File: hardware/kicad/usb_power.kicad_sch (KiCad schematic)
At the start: 14 parts, among them J1 U262-161N-4BVC11, U6 USBLC6-2P6, U7 MCP73831T-2ACI/OT

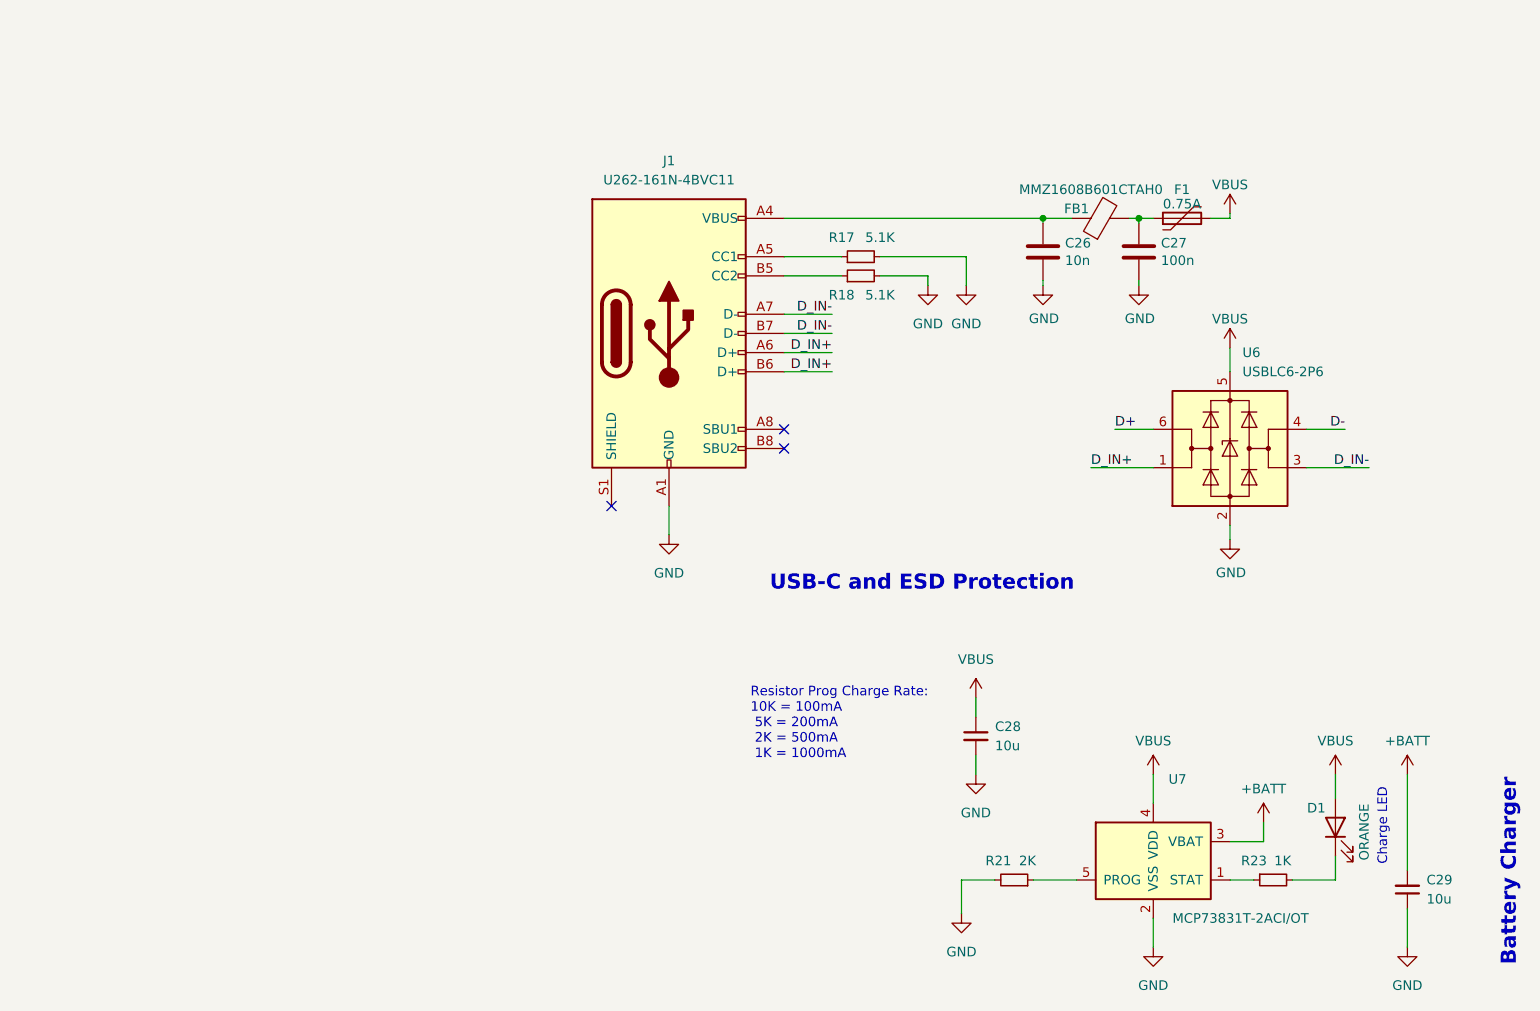
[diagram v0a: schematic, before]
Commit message: fix label
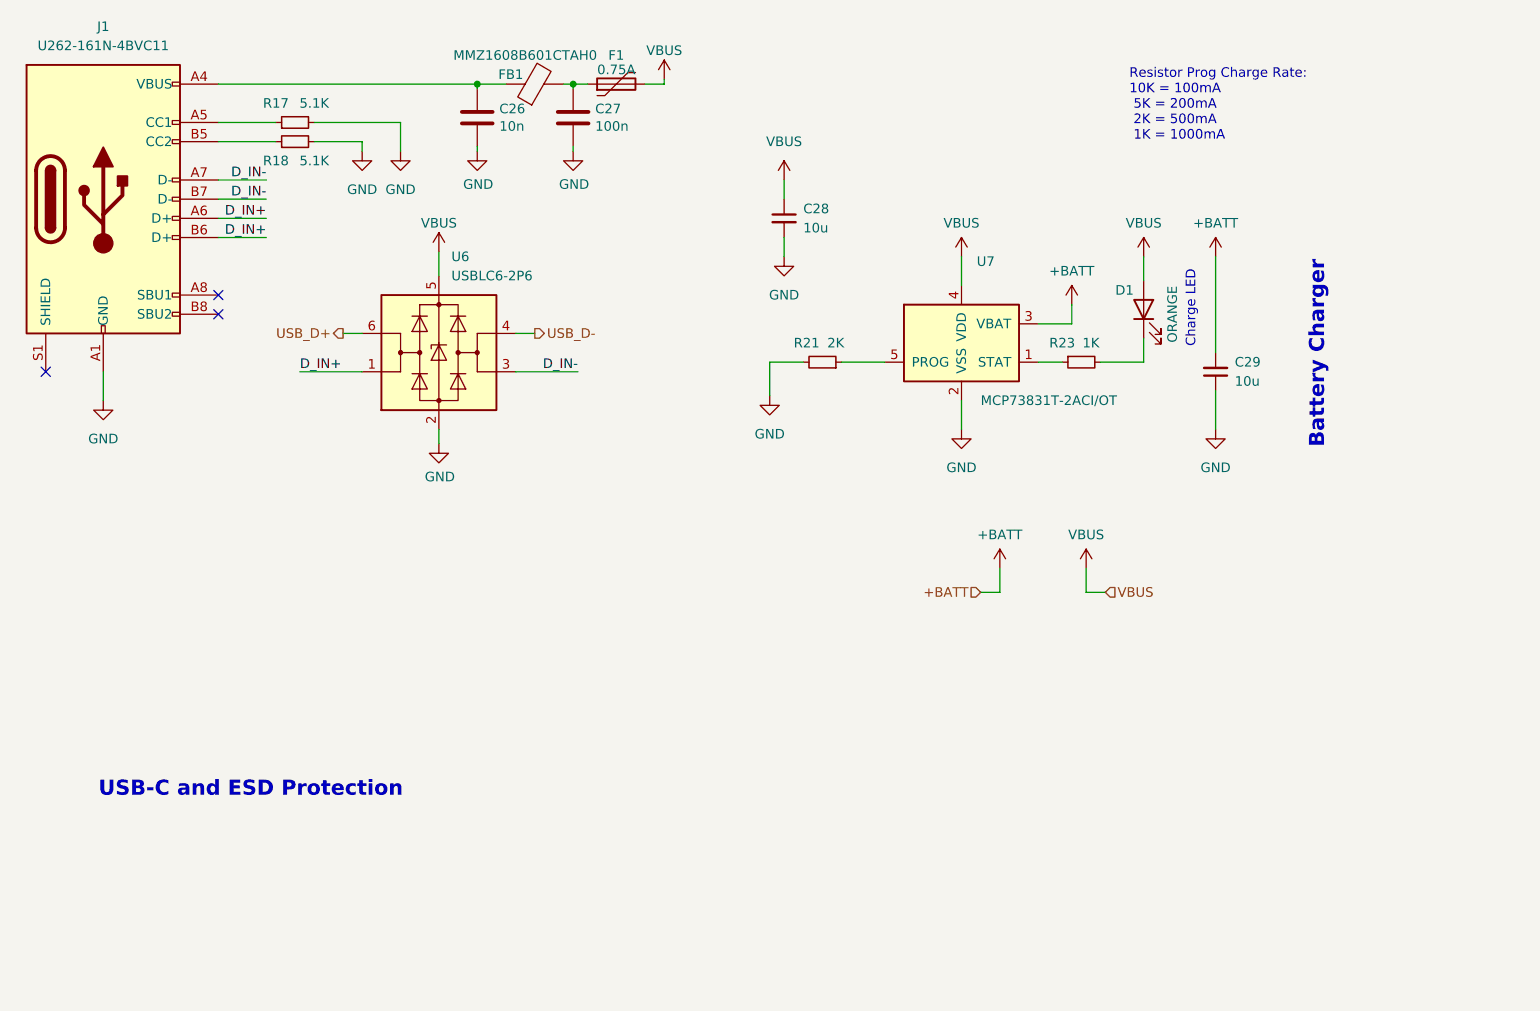
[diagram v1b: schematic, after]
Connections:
- net D+ renamed USB_D+
- net D- renamed USB_D-
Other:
- moved on the sheet: C26, C27, C28, C29, D1, F1, FB1, J1, R17, R18, R21, R23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

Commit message: beautify schematic
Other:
- note added: "Charge Rate: 500mA"
- note added: "Sheets Connection"
- note removed: "Resistor Prog Charge Rate: 10K = 100mA 5K = 200mA 2K = 500mA 1K = 1000mA"
- moved on the sheet: C26, C27, C28, C29, D1, F1, FB1, J1, R17, R18, R21, R23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

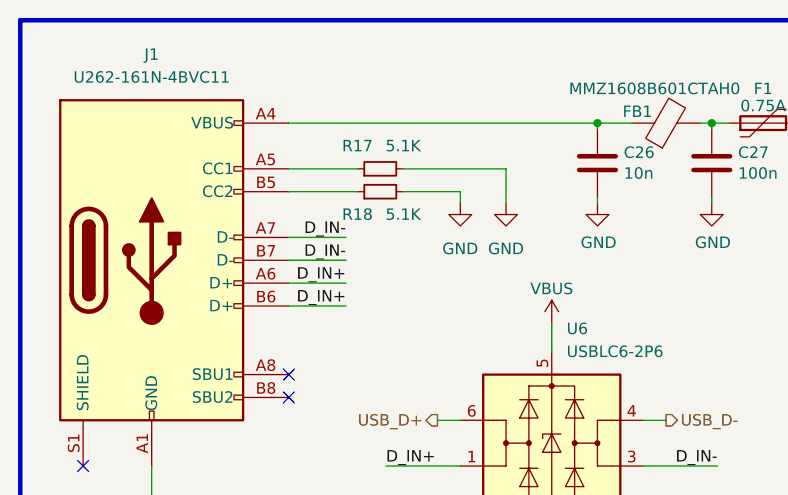
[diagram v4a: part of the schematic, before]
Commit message: usb power schematic partially done
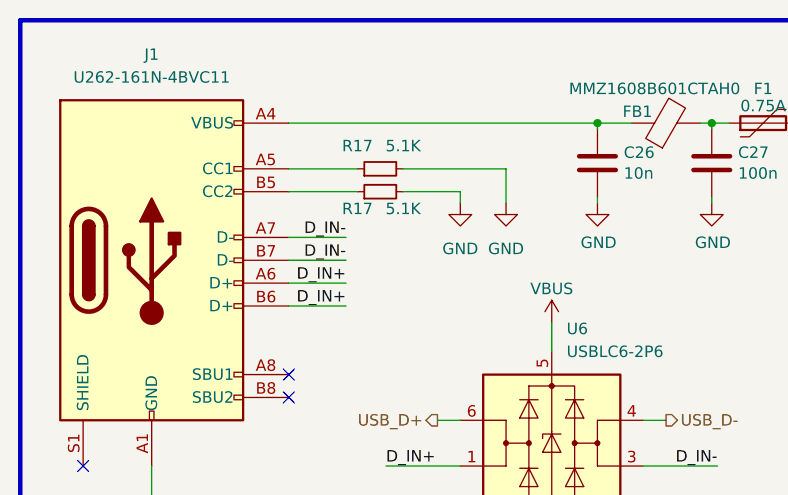
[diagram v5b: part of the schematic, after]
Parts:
- removed R18: 5.1K, Resistor_SMD:R_0402_1005Metric, symbol Device:R_Small
- added R17: 5.1K, Resistor_SMD:R_0402_1005Metric, symbol Device:R_Small
- C26: Distributor (none) -> LCSC; Distributor Link (none) -> https://www.lcsc.com/product-detail/Multilayer-Ceramic-Capa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; Distributor Part Number (none) -> C60133; Manufacturer Part Number (none) -> CC0402KRX7R9BB103; Part Description Ceramic Capacitor 10nF 10% 50V X7R -> Ceramic Capacitors 50V 10nF X7R ±10%; Part Number CC0402KRX7R9BB103 -> (none)
- C27: Distributor (none) -> LCSC; Distributor Link (none) -> https://www.lcsc.com/product-detail/Multilayer-Ceramic-Capa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; Distributor Part Number (none) -> C129131; Manufacturer Part Number (none) -> CC0402KRX5R6BB104; Part Description Ceramic Capacitor 100nF 10% 10V X5R -> Ceramic Capacitor 10V 100nF X5R ±10% 0402; Part Number CC0402KRX5R6BB104 -> (none)
- F1: Distributor (none) -> LCSC; Distributor Link (none) -> https://www.lcsc.com/product-detail/Resettable-Fuses_RUILON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; Distributor Part Number (none) -> C20979; Manufacturer RUILON -> RUILON(Shenzhen Ruilongyuan Elec); Manufacturer Part Number (none) -> SMD0805P075TF; Part Number SMD0805P075TF -> (none)
- FB1: Distributor (none) -> LCSC; Distributor Link (none) -> https://www.lcsc.com/product-detail/Ferrite-Beads_TDK-MMZ16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; Distributor Part Number (none) -> C97120; Manufacturer Part Number (none) -> MMZ1608B601CTAH0; Part Description (none) -> Ferrite Beads 400mΩ ±25% 600Ω@100MHz; Part Number MMZ1608B601CTAH0 -> (none)
- J1: footprint bwlr1e_prog:USB_C_Receptacle_XKB_U262-16XN-4BVC11 -> plantpal:USB_C_Receptacle_XKB_U262-16XN-4BVC11; Distributor (none) -> LCSC; Distributor Link (none) -> https://www.lcsc.com/product-detail/USB-Connectors_XKB-Conn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; Distributor Part Number (none) -> C319148; Manufacturer Part Number (none) -> U262-161N-4BVC11; Part Description (none) -> USB Connectors Type-C 3A USB 3.1 16P; Part Number U262-161N-4BVC11 -> (none)
- R17: Distributor (none) -> LCSC; Distributor Link (none) -> https://www.lcsc.com/product-detail/Chip-Resistor-Surface-M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; Distributor Part Number (none) -> C25905; Manufacturer (none) -> UNI-ROYAL(Uniroyal Elec); Manufacturer Part Number (none) -> 0402WGF5101TCE; Part Description Resistor 5.1K 1% 62.5mW -> Resistor 62.5mW ±1% 5.1kΩ
- U6: Distributor (none) -> LCSC; Distributor Link (none) -> https://www.lcsc.com/product-detail/ESD-Protection-Devices_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; Distributor Part Number (none) -> C15999; Manufacturer Part Number (none) -> USBLC6-2P6; Part Description (none) -> ESD Protection 6V 17V 2 Unidirectional 5.25V; Part Number USBLC6-2P6 -> (none)
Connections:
- net GND: now also R17.2
- net at J1.B5 (CC2): now also R17.1

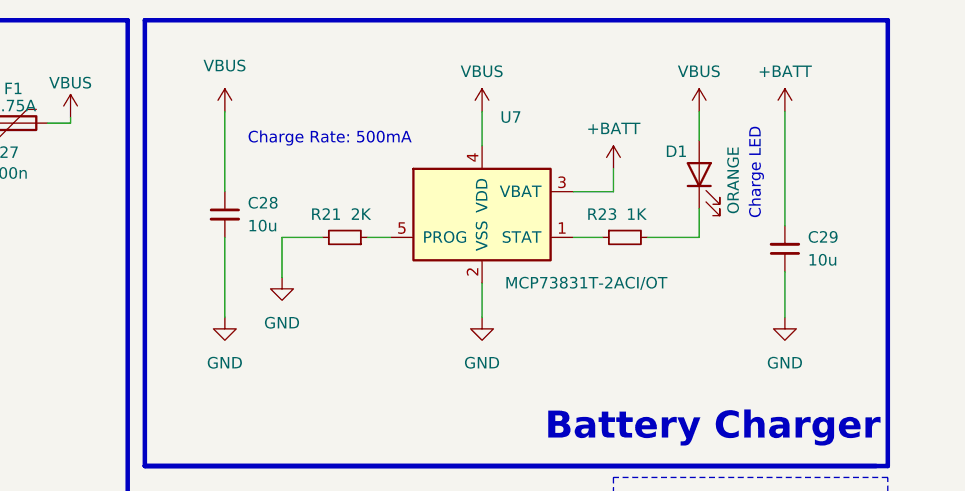
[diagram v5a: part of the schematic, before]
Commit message: usb power schematic done
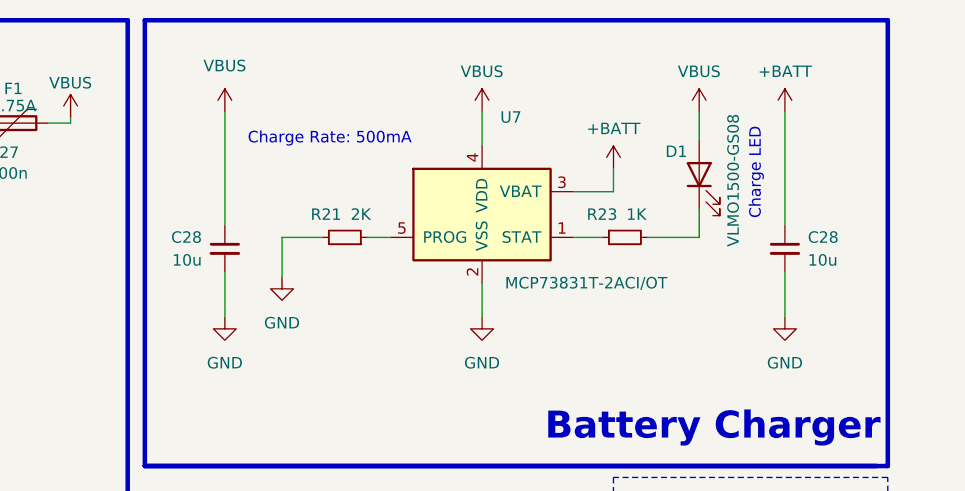
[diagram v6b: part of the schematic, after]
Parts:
- removed C29: 10u, Capacitor_SMD:C_0805_2012Metric, symbol Device:C_Small
- added C28: 10u, Capacitor_SMD:C_0603_1608Metric, symbol Device:C_Small
- C28: Distributor (none) -> LCSC; Distributor Link (none) -> https://www.lcsc.com/product-detail/Multilayer-Ceramic-Capa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; Distributor Part Number (none) -> C19702; Manufacturer (none) -> Samsung Electro-Mechanics; Manufacturer Part Number (none) -> CL10A106KP8NNNC; Part Description Ceramic Capacitor 10uF 10% 10V X5R -> Ceramic Capacitor 10V 10uF X5R ±10% 0603
- D1: value ORANGE -> VLMO1500-GS08; Distributor (none) -> LCSC; Distributor Link (none) -> https://www.lcsc.com/product-detail/Light-Emitting-Diodes-s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; Distributor Part Number (none) -> C3000857; Manufacturer (none) -> Vishay Intertech; Manufacturer Part Number (none) -> VLMO1500-GS08; Part Description Orange 2V 25mA -> Orange 2V 20mA
- R21: footprint Resistor_SMD:R_0603_1608Metric -> Resistor_SMD:R_0402_1005Metric; Distributor (none) -> LCSC; Distributor Link (none) -> https://www.lcsc.com/product-detail/Chip-span-style-backgro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; Distributor Part Number (none) -> C4109; Manufacturer (none) -> UNI-ROYAL(Uniroyal Elec); Manufacturer Part Number (none) -> 0402WGF2001TCE; Part Description Resistor 2K 1% 100mW -> Resistor 62.5mW ±1% 2kΩ
- R23: footprint Resistor_SMD:R_0603_1608Metric -> Resistor_SMD:R_0402_1005Metric; Distributor (none) -> LCSC; Distributor Link (none) -> https://www.lcsc.com/product-detail/Chip-span-style-backgro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; Distributor Part Number (none) -> C11702; Manufacturer (none) -> UNI-ROYAL(Uniroyal Elec); Manufacturer Part Number (none) -> 0402WGF1001TCE; Part Description Resistor 1k 5% 100mW -> Resistor 62.5mW ±1% 1kΩ
- U7: Distributor (none) -> Mouser; Distributor Link (none) -> https://www.mouser.com/ProductDetail/Microchip-Technology/M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; Distributor Part Number (none) -> 579-MCP73831T-2ACIOT; Manufacturer Microchip -> Microchip Technology; Manufacturer Part Number (none) -> MCP73831T-2ACI/OT; Part Description (none) -> Battery Management IC 6V LiPoly 1500mA; Part Number MCP73831T-2ACI/OT -> (none)
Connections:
- net +BATT: now also C28.1
- net GND: now also C28.2
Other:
- moved on the sheet: C28

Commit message: clean-up
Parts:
- removed C26: 10n, Capacitor_SMD:C_0402_1005Metric, symbol Device:C
- added C12: 10n, Capacitor_SMD:C_0402_1005Metric, symbol Device:C
- C27: Distributor Link https://www.lcsc.com/product-detail/Multilayer-Ceramic-Capacitors-MLCC-SMD-SMT_YAGEO-CC0402KRX5R6BB104_C129131.html -> https://www.lcsc.com/product-detail/Multilayer-Ceramic-Capacitors-MLCC-SMD-SMT_Samsung-Electro-Mechanics-CL05B104KO5NNNC_C1525.html; Distributor Part Number C129131 -> C1525; Manufacturer YAGEO -> Samsung Electro-Mechanics; Manufacturer Part Number CC0402KRX5R6BB104 -> CL05B104KO5NNNC; Part Description Ceramic Capacitor 10V 100nF X5R ±10% 0402 -> Ceramic Capacitor 16V 100nF X7R ±10%
- R17: value 5.1K -> 5K1
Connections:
- net GND: now also C12.2
- net at FB1.1, J1.A4 (VBUS), J1.A9 (VBUS)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: now also C12.1
